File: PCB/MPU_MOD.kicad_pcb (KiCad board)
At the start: 8 copper layers, 43.5 x 70 mm, 266 parts, among them J1 SJ-43504-SMT-TR, J2 2-1734248-0, J3 USB4510-03-1-A_REVA, J501 MEM2090-00-145-00-A_REVA, J701 FTSH-107-01-L-DV-K-A, J901 73412-0110, U1 IS21ES08GA-JQLI-TR, U201 STC3115IQT, U203 STPMIC1APQR, U3 BQ24298RTWR, U301 STM32MP157FABx, U401 MT41K256M16TW-107_P, U502 HSP051-4M10, U503 HSP051-4M10, U701 HSP051-4M10, U702 HSP051-4M10, U801 FUSB302BMPX, U802 HSP051-4M10, U901 LBEE5PK2AE-771, Y601 NX2012SA-32.768K, Y701 ECS-2520MVQ-240

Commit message: PCB_UPDATE
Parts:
- removed D701: PTVS3V3S1UR, lib:TVS_PTVS3V3S1UR
- removed R702, R703: 0, Resistor_SMD:R_0402_1005Metric
- removed S604, S605: EVQ-9P701P, lib:SW_EVQ-9P701P
- added C1: 1uF, lib:C_0402_small, B.Cu at (67.2, 65.7)
- added C2: 1uF, lib:C_0402_small, B.Cu at (67.2, 67.5)
- added C3: 1uF, lib:C_0402_small, B.Cu at (67.2, 68.5)
- added C4: 1uF, lib:C_0402_small, B.Cu at (84.5, 65.7)
- added C5: 1uF, lib:C_0402_small, B.Cu at (81.3, 72.9)
- added C6: 1uF, lib:C_0402_small, B.Cu at (82.9, 72.9)
- added C7: 1uF, lib:C_0402_small, B.Cu at (84.5, 70.4)
- added C8: 1nF, lib:C_0402_small, B.Cu at (84.4, 68.2)
- added C9: 1nF, lib:C_0402_small, B.Cu at (84.5, 72.9)
- added D3: MSP3V3-M3/89A, Diode_SMD:D_MicroSMP_KA, F.Cu at (72.7, 57.8)
- added TP201: TestPoint, lib:TP_0.5, B.Cu at (29.3, 68.1)
- added TP202: TestPoint, lib:TP_0.5, B.Cu at (29.3, 69.6)
- added TP204: TestPoint, lib:TP_0.5, B.Cu at (29.3, 71.1)
- added TP205: TestPoint, lib:TP_0.5, B.Cu at (29.3, 72.6)
- added TP206: TestPoint, lib:TP_0.5, B.Cu at (30.8, 68.1)
- added TP207: TestPoint, lib:TP_0.5, B.Cu at (30.8, 69.6)
- added TP208: TestPoint, lib:TP_0.5, B.Cu at (30.8, 71.1)
- added TP209: TestPoint, lib:TP_0.5, B.Cu at (30.8, 72.6)
- added TP210: TestPoint, lib:TP_0.5, B.Cu at (32.3, 68.1)
- added TP211: TestPoint, lib:TP_0.5, B.Cu at (32.3, 69.6)
- added TP212: TestPoint, lib:TP_0.5, B.Cu at (32.3, 71.1)
- added TP401: TestPoint, lib:TP_0.5, B.Cu at (25.8, 77.6)
- added TP402: TestPoint, lib:TP_0.5, B.Cu at (25.8, 79.1)
- added TP403: TestPoint, lib:TP_0.5, B.Cu at (25.8, 80.6)
- added TP601: TestPoint, lib:TP_0.5, B.Cu at (20.8, 77.6)
- added TP602: TestPoint, lib:TP_0.5, B.Cu at (20.8, 79.1)
- added TP701: TestPoint, lib:TP_0.5, B.Cu at (20.8, 68.1)
- added TP702: TestPoint, lib:TP_0.5, B.Cu at (20.8, 69.6)
- added TP703: TestPoint, lib:TP_0.5, B.Cu at (52.2, 98.0)
- added TP704: TestPoint, lib:TP_0.5, B.Cu at (53.7, 98.0)
- added TP705: TestPoint, lib:TP_0.5, B.Cu at (55.2, 98.0)
- added TP706: TestPoint, lib:TP_0.5, B.Cu at (54.1, 89.5)
- added TP707: TestPoint, lib:TP_0.5, B.Cu at (55.6, 89.5)
- added TP708: TestPoint, lib:TP_0.5, B.Cu at (57.1, 89.5)
- added TP709: TestPoint, lib:TP_0.5, B.Cu at (58.6, 89.5)
- added TP710: TestPoint, lib:TP_0.5, B.Cu at (54.5, 98.5)
- added TP801: TestPoint, lib:TP_0.5, B.Cu at (25.8, 68.1)
- added TP803: TestPoint, lib:TP_0.5, B.Cu at (25.8, 69.6)
- added TP804: TestPoint, lib:TP_0.5, B.Cu at (25.8, 71.1)
- added TP805: TestPoint, lib:TP_0.5, B.Cu at (25.8, 72.6)
- added TP806: TestPoint, lib:TP_0.5, B.Cu at (25.8, 74.1)
- added TP901: TestPoint, lib:TP_0.5, B.Cu at (29.3, 76.1)
- added TP902: TestPoint, lib:TP_0.5, B.Cu at (29.3, 77.6)
- added TP903: TestPoint, lib:TP_0.5, B.Cu at (30.8, 76.1)
- added TP904: TestPoint, lib:TP_0.5, B.Cu at (30.8, 77.6)
- added TP905: TestPoint, lib:TP_0.5, B.Cu at (32.3, 76.1)
- added TP906: TestPoint, lib:TP_0.5, B.Cu at (32.3, 77.6)
- added TP907: TestPoint, lib:TP_0.5, B.Cu at (33.8, 76.1)
- added TP908: TestPoint, lib:TP_0.5, B.Cu at (33.8, 77.6)
- D203: value PTVS3V3S1UR -> MSP3V3-M3/89A; footprint lib:TVS_PTVS3V3S1UR -> Diode_SMD:D_MicroSMP_KA
- J701, R701: moved to B.Cu
- TP203, TP802: footprint Library:TP_0.5mm -> lib:TP_0.5
- moved R715 44.8 mm to (58.1, 98.0)
- moved U702 43.1 mm to (57.6, 96.0)
- moved U701 42.1 mm to (55.7, 92.2)
- moved J701 41.9 mm to (55.2, 93.7), turned to 180 degrees
- moved R701 35.3 mm to (70.2, 56.7), turned to 180 degrees
- moved S701 24.9 mm to (70.0, 56.5), turned to -90 degrees
- moved D2 24.4 mm to (82.0, 99.9)
- moved R221 24.4 mm to (83.0, 98.0)
- moved D1 24.4 mm to (82.0, 98.0)
- moved R220 24.4 mm to (83.0, 99.9)
- moved TP203 15.9 mm to (37.4, 73.8)
- moved C701 14.9 mm to (38.1, 59.3)
- moved C702 14.9 mm to (38.1, 61.3)
- moved S601 9.20 mm to (62.2, 61.3), turned to 0 degrees
- moved C305 8.53 mm to (82.9, 71.3)
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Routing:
- net GND: track 91.1 -> 181.3 mm, vias 88 -> 118
- net VDD_CORE: track 15.6 -> 58.8 mm, vias 14 -> 25
- net VDD: track 6.06 -> 29.5 mm, vias 14 -> 25
- net Net-(U301A-VBAT): track 0.00 -> 9.01 mm, vias 0 -> 2
- net /RCC_BOOT_RST_DEBUG/OSC_OUT: track 0.00 -> 8.74 mm
- net Net-(D602-K): track 0.00 -> 7.96 mm, vias 0 -> 2
- net PWR_ON: track 2.16 -> 9.91 mm, vias 1 -> 3
- net Net-(U301C-PC15): track 0.00 -> 7.07 mm
- net Net-(D601-K): track 0.00 -> 5.84 mm, vias 0 -> 2
- net /MPU_PWR/VDDA: track 2.16 -> 7.60 mm, vias 1 -> 3
- net Net-(U301C-PC14): track 0.00 -> 5.03 mm
- net Net-(Y701-Tri-State): track 0.00 -> 3.82 mm
- net /RCC_BOOT_RST_DEBUG/OSC_IN: track 0.00 -> 3.72 mm
- net VDD_DDR: track 45.7 -> 48.0 mm, vias 28 -> 30
- net Net-(Y701-VDD): track 0.00 -> 1.39 mm
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
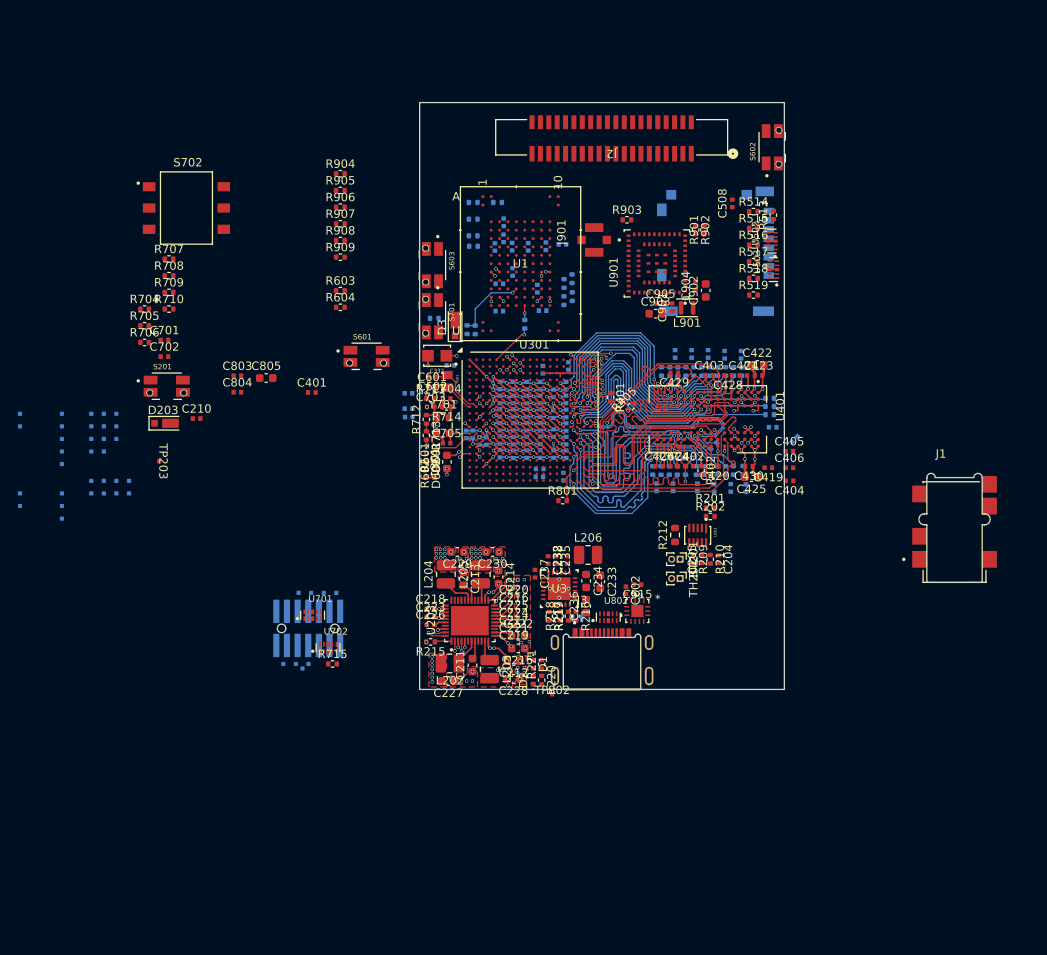
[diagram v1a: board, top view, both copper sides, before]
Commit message: PCB_UPDATE SD CARD DONE
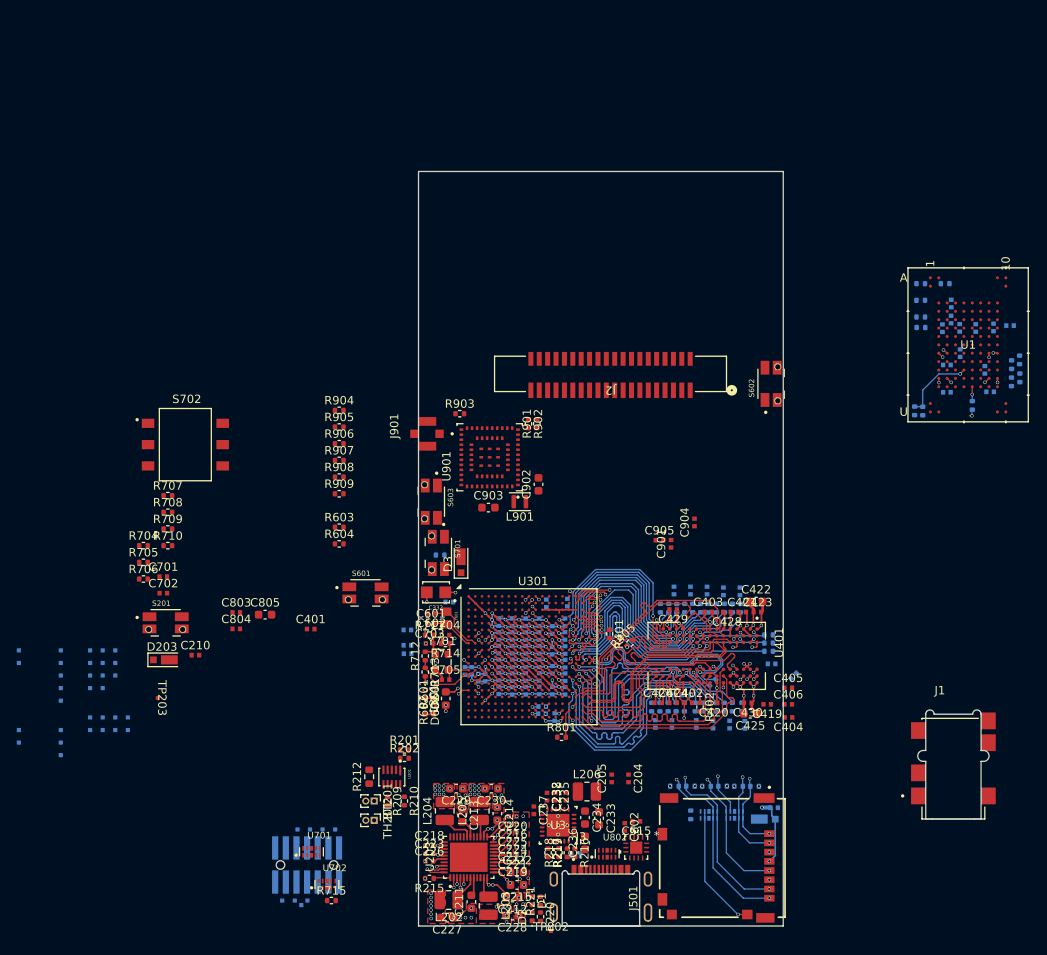
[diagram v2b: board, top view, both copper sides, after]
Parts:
- added D4: MSP3V3-M3/89A, Diode_SMD:D_MicroSMP_KA, B.Cu at (109.9, 116.5)
- added NT1: NetTie_2, NetTie:NetTie-2_SMD_Pad0.5mm, B.Cu at (109.8, 115.1)
- C508, R513, R514, R515, R516, R517, R518, R519, U502, U503: moved to B.Cu
- J501: moved to F.Cu
- moved J501 72.4 mm to (112.1, 121.1), turned to 90 degrees
- moved C508 72.3 mm to (110.8, 115.1), turned to 180 degrees
- moved R513 72.2 mm to (100.8, 116.0)
- moved U502 68.8 mm to (103.0, 116.0), turned to 180 degrees
- moved R514 68.6 mm to (108.5, 112.6)
- moved R515 66.6 mm to (106.5, 112.5), turned to 180 degrees
- moved U503 65.2 mm to (106.1, 116.0), turned to 180 degrees
- moved R516 64.7 mm to (104.6, 112.5)
- moved R517 62.8 mm to (102.7, 112.5), turned to 180 degrees
- moved R518 61.0 mm to (100.8, 112.5)
- moved R519 59.3 mm to (98.9, 112.5), turned to 180 degrees
- moved U1 54.3 mm to (133.9, 59.9)
- moved C503 54.3 mm to (132.9, 57.9)
- moved C506 54.3 mm to (133.0, 60.9)
- moved C509 54.3 mm to (131.9, 55.0)
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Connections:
- C508 pad 2: 3V3 -> Net-(J501-VDD)
- J501 pad P4: 3V3 -> Net-(J501-VDD)
- U502 pad 1: SDMMC1_CMD -> SDMMC1_D0
- U502 pad 10: SDMMC1_CMD -> SDMMC1_D0
- U502 pad 2: SDMMC1_CK -> SDMMC1_D1
- U502 pad 5: Net-(U502-I/O_4) -> unconnected-(U502-I/O_4-Pad5)
- U502 pad 6: Net-(U502-I/O_4) -> unconnected-(U502-I/O_4-Pad5)
- U502 pad 9: SDMMC1_CK -> SDMMC1_D1
- U503 pad 4: SDMMC1_D0 -> SDMMC1_CMD
- U503 pad 5: SDMMC1_D1 -> SDMMC1_CK
- U503 pad 6: SDMMC1_D1 -> SDMMC1_CK
- U503 pad 7: SDMMC1_D0 -> SDMMC1_CMD
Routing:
- net SDMMC1_D1: track 0.00 -> 59.0 mm, vias 0 -> 3
- net SDMMC1_D0: track 0.00 -> 56.8 mm, vias 0 -> 3
- net SDMMC1_CK: track 0.00 -> 54.6 mm, vias 0 -> 3
- net SDMMC1_D3: track 0.00 -> 53.3 mm, vias 0 -> 3
- net SDMMC1_D2: track 0.00 -> 53.1 mm, vias 0 -> 3
- net SDMMC1_CMD: track 0.00 -> 45.3 mm, vias 0 -> 3
- net Net-(J501-SWITCH): track 0.00 -> 15.0 mm, vias 0 -> 1
- net SDMMC2_D6: track 13.1 -> 5.95 mm, vias 2 -> 1
- net Net-(J501-VDD): track 0.00 -> 6.98 mm, vias 0 -> 1
- net SDMMC2_D3: track 9.44 -> 3.55 mm, vias 2 -> 1
- net SDMMC2_D1: track 8.72 -> 3.70 mm, vias 2 -> 1
- net SDMMC2_D5: track 14.0 -> 9.04 mm, vias 2 -> 1
- net SDMMC2_CK: track 5.30 -> 1.06 mm
- net SDMMC2_D7: track 15.5 -> 11.4 mm, vias 2 -> 1
- net SDMMC2_D2: track 13.2 -> 9.03 mm, vias 2 -> 1
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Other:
- board size 43.5 x 70 mm -> 43.5 x 90 mm

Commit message: PCB_UPDATE
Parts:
- C803, C804, TP802: moved to B.Cu
- moved C803 49.1 mm to (87.2, 119.5), turned to 180 degrees
- moved C804 48.5 mm to (87.2, 120.4)
- moved C805 45.1 mm to (82.7, 123.2), turned to 90 degrees
- moved C205 29.1 mm to (62.5, 108.2)
- moved C204 29.0 mm to (64.7, 108.2)
- moved R219 9.42 mm to (88.5, 112.3), turned to 90 degrees
- moved TP802 9.19 mm to (88.4, 121.6), turned to 180 degrees
- moved R218 8.39 mm to (87.2, 112.3), turned to -90 degrees
- moved R216 8.32 mm to (85.3, 112.3), turned to 90 degrees
- moved C237 8.29 mm to (90.2, 117.4), turned to 90 degrees
- moved R217 8.14 mm to (86.2, 112.3), turned to -90 degrees
- moved L206 7.72 mm to (83.8, 119.3), turned to 180 degrees
- moved C233 7.32 mm to (82.6, 116.5), turned to 90 degrees
- moved C238 7.27 mm to (88.7, 119.1), turned to 90 degrees
- moved C236 7.08 mm to (84.1, 113.5), turned to -90 degrees
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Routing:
- net USB_D-: track 0.00 -> 31.5 mm, vias 0 -> 2
- net USB_D+: track 0.00 -> 30.6 mm, vias 0 -> 2
- net GND: track 183.7 -> 188.9 mm, vias 122 -> 130
- net V_USB: track 0.00 -> 3.65 mm, vias 0 -> 3
- net Net-(U301A-VDDA1V8_DSI): track 1.39 -> 0.57 mm
- net Net-(U301A-VDDA1V1_REG): track 1.39 -> 0.58 mm
- net VDD_USB: track 4.34 -> 5.08 mm
- net VIN: vias 9 -> 21
- added copper zone on F.Cu, net VIN
